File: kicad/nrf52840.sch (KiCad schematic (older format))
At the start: 16 parts, among them J1 Conn_01x02, J2 Conn_01x04, J3 Conn_01x06, J4 Conn_01x10, SW1 SW_Push, U1 NRF52840_MS88SF2, U2 AMS1117-3.3, U3 LM2902

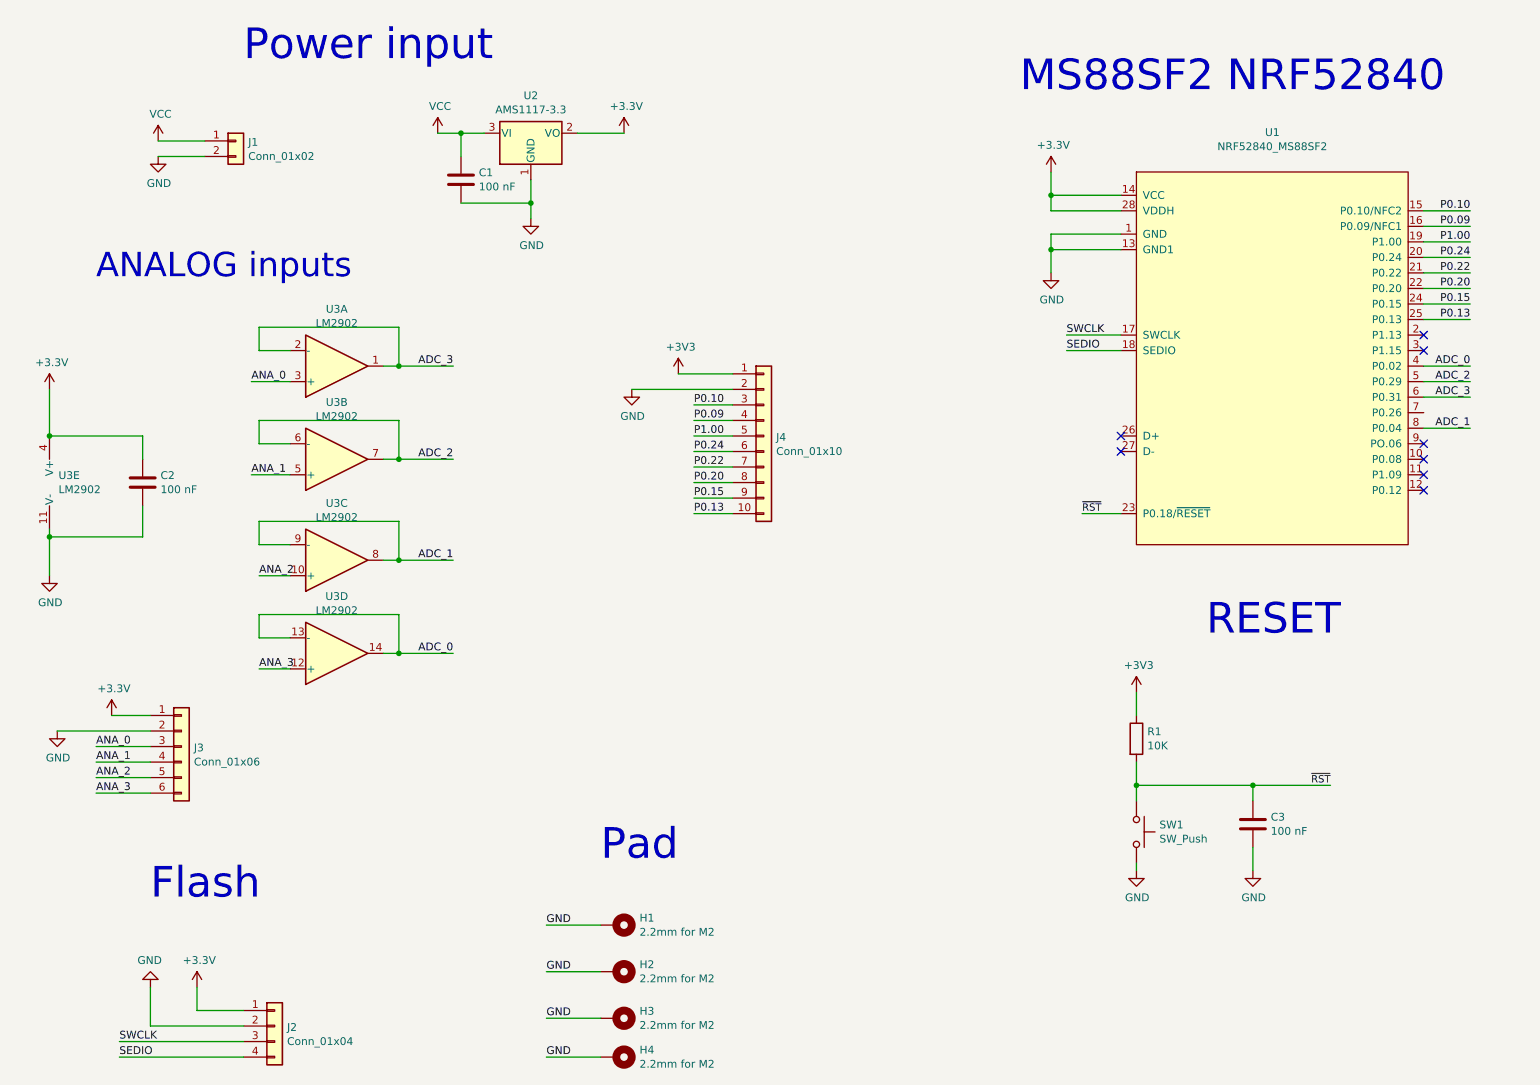
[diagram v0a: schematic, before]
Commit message: add resistors for input analogs
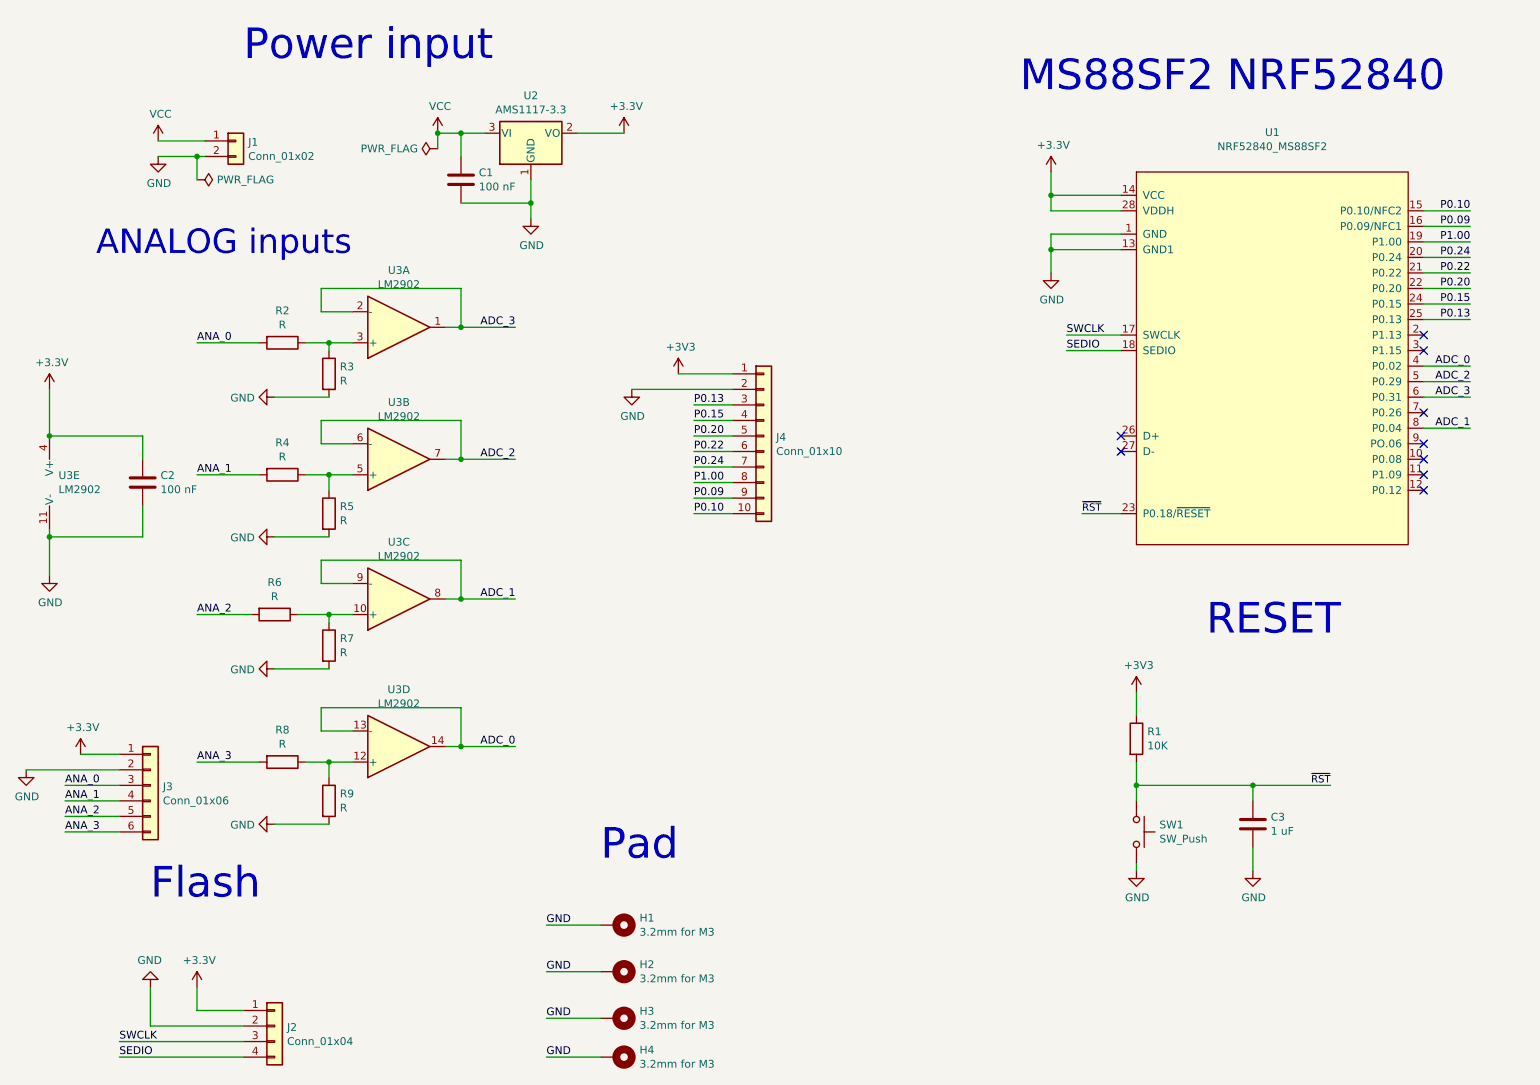
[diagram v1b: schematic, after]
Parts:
- added R2, R3, R4, R5, R6, R7, R8, R9: R, Capacitor_SMD:C_0805_2012Metric_Pad1.18x1.45mm_HandSolder, symbol Device:R
- C3: value 100 nF -> 1 uF
- H1, H2, H3, H4: value 2.2mm for M2 -> 3.2mm for M3; footprint MountingHole:MountingHole_2.2mm_M2_Pad -> MountingHole:MountingHole_3.2mm_M3_Pad_Via
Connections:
- net ANA_0: now also R2.2; no longer U3.3 (+)
- net ANA_1: now also R4.2; no longer U3.5 (+)
- net ANA_2: now also R6.2; no longer U3.10 (+)
- net ANA_3: now also R8.2; no longer U3.12 (+)
- net GND: now also R3.2, R5.2, R7.2, R9.2
- net P0.09: now also J4.9 (Pin_9); no longer J4.4 (Pin_4)
- net P0.10: now also J4.10 (Pin_10); no longer J4.3 (Pin_3)
- net P0.13: now also J4.3 (Pin_3); no longer J4.10 (Pin_10)
- net P0.15: now also J4.4 (Pin_4); no longer J4.9 (Pin_9)
- net P0.20: now also J4.5 (Pin_5); no longer J4.8 (Pin_8)
- net P0.22: now also J4.6 (Pin_6); no longer J4.7 (Pin_7)
- net P0.24: now also J4.7 (Pin_7); no longer J4.6 (Pin_6)
- net P1.00: now also J4.8 (Pin_8); no longer J4.5 (Pin_5)
- new net: R2.1, R3.1, U3.3 (+)
- new net: R4.1, R5.1, U3.5 (+)
- new net: R6.1, R7.1, U3.10 (+)
- new net: R8.1, R9.1, U3.12 (+)
- no-connect marks 8 -> 9
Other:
- moved on the sheet: J3, U3A, U3B, U3C, U3D

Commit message: update
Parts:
- J1: footprint Connector_JST:JST_XH_S2B-XH-A_1x02_P2.50mm_Horizontal -> Connector_JST:JST_XH_S2B-XH-A-1_1x02_P2.50mm_Horizontal
- SW1: footprint Button_Switch_SMD:SW_Push_1P1T_NO_CK_KMR2 -> Button_Switch_SMD:SW_SPST_SKQG_WithStem
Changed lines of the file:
@@
-$EndComp
-$Comp
-L Connector_Generic:Conn_01x02 J1
-U 1 1 604A0BE3
-P 2050 1400
-F 0 "J1" H 2130 1392 50  0000 L CNN
-F 1 "Conn_01x02" H 2130 1301 50  0000 L CNN
-F 2 "Connector_JST:JST_XH_S2B-XH-A_1x02_P2.50mm_Horizontal" H 2130 1255 50  0001 L CNN
-F 3 "~" H 2050 1400 50  0001 C CNN
-	1    2050 1400
-	1    0    0    -1
 $EndComp
 $Comp
@@
 F 0 "SW1" V 7804 5998 50  0000 L CNN
 F 1 "SW_Push" V 7895 5998 50  0000 L CNN
-F 2 "Button_Switch_SMD:SW_Push_1P1T_NO_CK_KMR2" H 7850 6050 50  0001 C CNN
+F 2 "Button_Switch_SMD:SW_SPST_SKQG_WithStem" H 7850 6050 50  0001 C CNN
 F 3 "~" H 7850 6050 50  0001 C CNN
 	1    7850 5850
@@
 Wire Wire Line
 	1800 1500 1850 1500
+$Comp
+L Connector_Generic:Conn_01x02 J1
+U 1 1 604A0BE3
+P 2050 1400
+F 0 "J1" H 2130 1392 50  0000 L CNN
+F 1 "Conn_01x02" H 2130 1301 50  0000 L CNN
+F 2 "Connector_JST:JST_XH_S2B-XH-A-1_1x02_P2.50mm_Horizontal" H 2130 1255 50  0001 L CNN
+F 3 "~" H 2050 1400 50  0001 C CNN
+	1    2050 1400
+	1    0    0    -1
+$EndComp
 $EndSCHEMATC
